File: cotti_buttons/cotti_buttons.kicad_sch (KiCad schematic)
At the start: 5 parts, among them J1 Pmod GPIO 1x06 pin

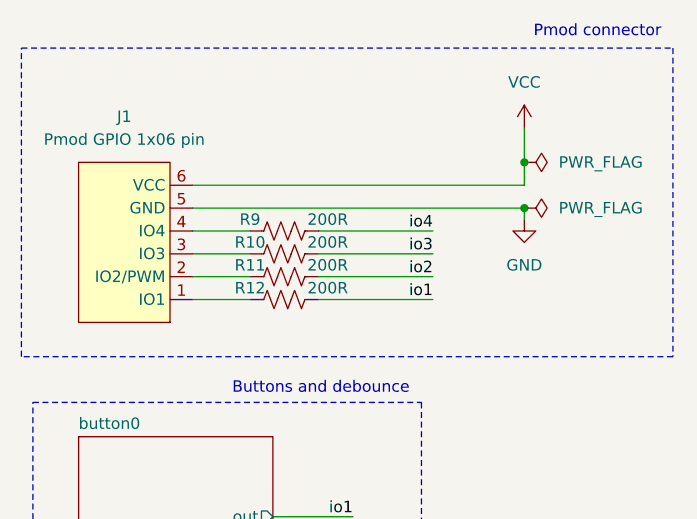
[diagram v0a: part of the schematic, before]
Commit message: feat: cotti uttons with new libs
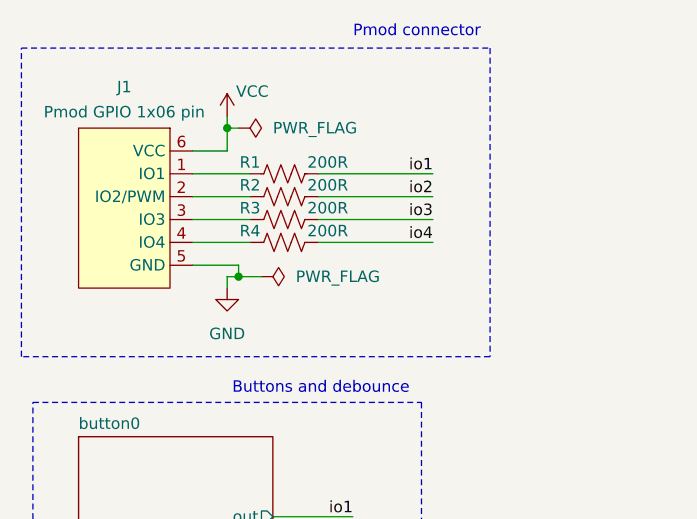
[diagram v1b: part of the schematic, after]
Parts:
- removed J1: Pmod GPIO 1x06 pin, Pmod:Pmod_1x06_pin, symbol Pmod:pmod_gpio_1x06_pin
- added J1: Pmod GPIO 1x06 pin, cotti_footprints:Pmod_1x06_pin, symbol cotti_pmod:pmod_gpio_1x06_pin
- renumbered R9 to R1, R10 to R2, R11 to R3, R12 to R4
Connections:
- net GND: now also J1.5 (GND)
- net VCC: now also J1.6 (VCC)
- net io1: now also R1.2; no longer R4.2
- net io2: now also R2.2; no longer R3.2
- net io3: now also R3.2; no longer R2.2
- net io4: now also R4.2; no longer R1.2
- net at R2.1: now also J1.2 (IO2/PWM)
- net at R4.1: now also J1.4 (IO4)
- net at R3.1: now also J1.3 (IO3)
- net at R1.1: now also J1.1 (IO1)
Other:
- moved on the sheet: R1, R2, R3, R4

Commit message: feat: cotti buttons gerber files
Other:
- company: (none) -> Cotti
- title: Cotti Button Module -> Button Module
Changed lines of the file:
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@@
 	(paper "A4")
 	(title_block
-		(title "Cotti Button Module")
-		(date "2025-12-18")
+		(title "Button Module")
+		(date "2026-01-17")
 		(rev "0.0")
+		(company "Cotti")
 	)
 	(rectangle
